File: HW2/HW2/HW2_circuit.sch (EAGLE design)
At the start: 23 parts, among them J1 PIC_ICSP_6_PIN, X1 MINI-USB_SHIELD5P2-32005-601

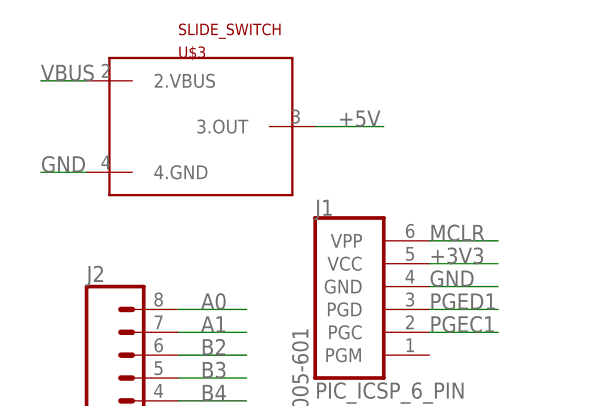
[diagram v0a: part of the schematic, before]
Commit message: Updated Library
Changed PICKIT to only have 5 through holes, modified switch connector
device to match data sheet, and changed switch and button symbols for
better illustration.
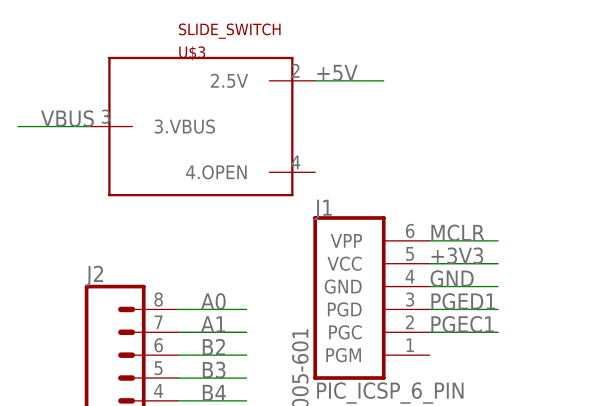
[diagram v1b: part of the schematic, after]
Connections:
- net +5V: now also U$3.2.5V; no longer U$3.3.OUT
- net GND: no longer U$3.4.GND
- net VBUS: now also U$3.3.VBUS; no longer U$3.2.VBUS
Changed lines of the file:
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@@
 </segment>
 <segment>
-<pinref part="U$3" gate="G$1" pin="3.OUT"/>
-<wire x1="-30.48" y1="60.96" x2="-22.86" y2="60.96" width="0.1524" layer="91"/>
-<label x="-27.94" y="60.96" size="1.778" layer="95"/>
+<pinref part="U$3" gate="G$1" pin="2.5V"/>
+<wire x1="-30.48" y1="66.04" x2="-22.86" y2="66.04" width="0.1524" layer="91"/>
+<label x="-30.48" y="66.04" size="1.778" layer="95"/>
 </segment>
 </net>
@@
 <label x="-15.24" y="5.08" size="1.778" layer="95"/>
 </segment>
-<segment>
-<pinref part="U$3" gate="G$1" pin="4.GND"/>
-<wire x1="-55.88" y1="55.88" x2="-60.96" y2="55.88" width="0.1524" layer="91"/>
-<label x="-60.96" y="55.88" size="1.778" layer="95"/>
-</segment>
 </net>
 <net name="OSC2" class="0">
@@
 </segment>
 <segment>
-<pinref part="U$3" gate="G$1" pin="2.VBUS"/>
-<wire x1="-55.88" y1="66.04" x2="-60.96" y2="66.04" width="0.1524" layer="91"/>
-<label x="-60.96" y="66.04" size="1.778" layer="95"/>
-</segment>
-</net>
+<pinref part="U$3" gate="G$1" pin="3.VBUS"/>
+<wire x1="-55.88" y1="60.96" x2="-63.5" y2="60.96" width="0.1524" layer="91"/>
+<label x="-60.96" y="60.96" size="1.778" layer="95"/>
+</segment>
+</net>

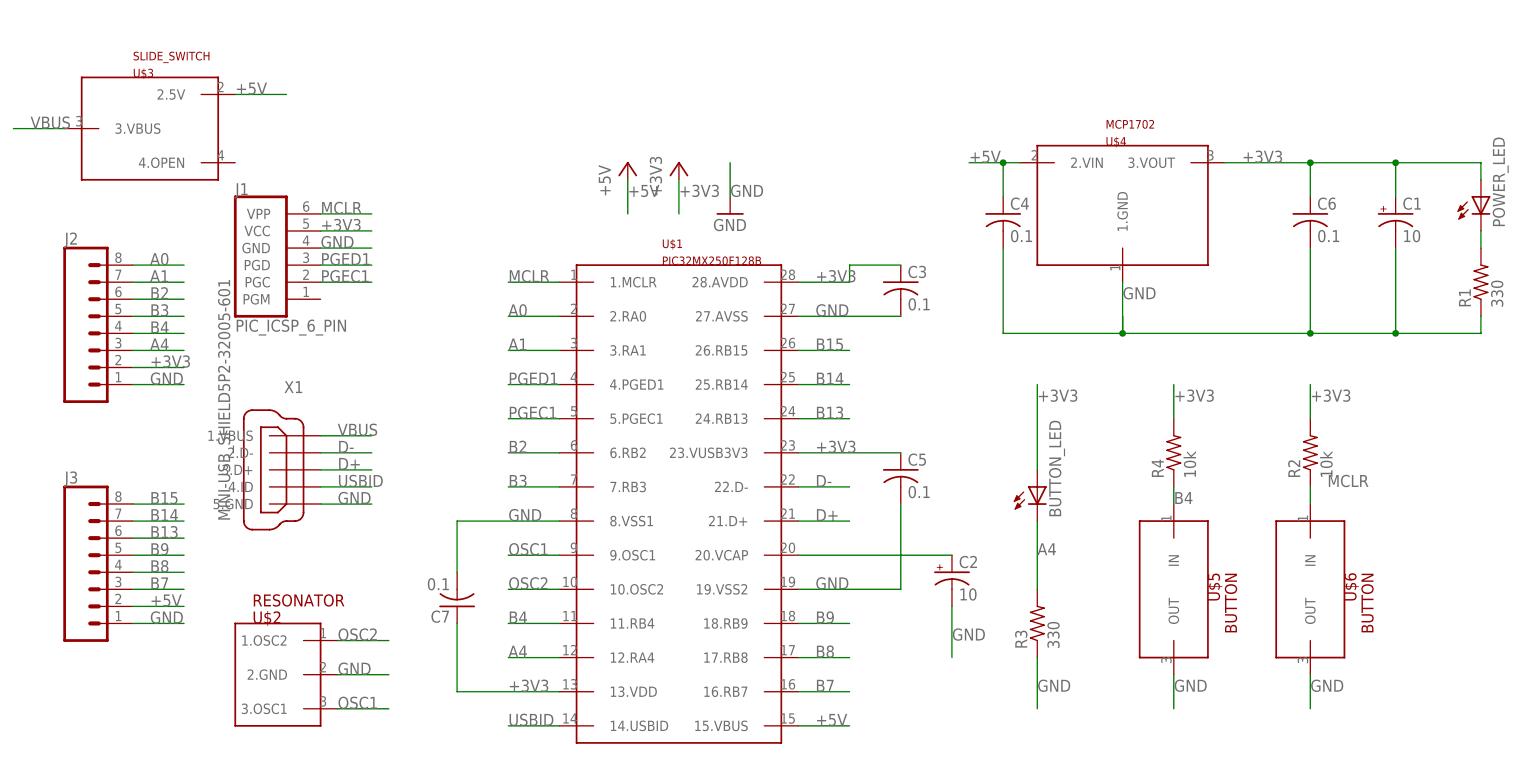
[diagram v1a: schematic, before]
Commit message: Updated Schematic Symbols
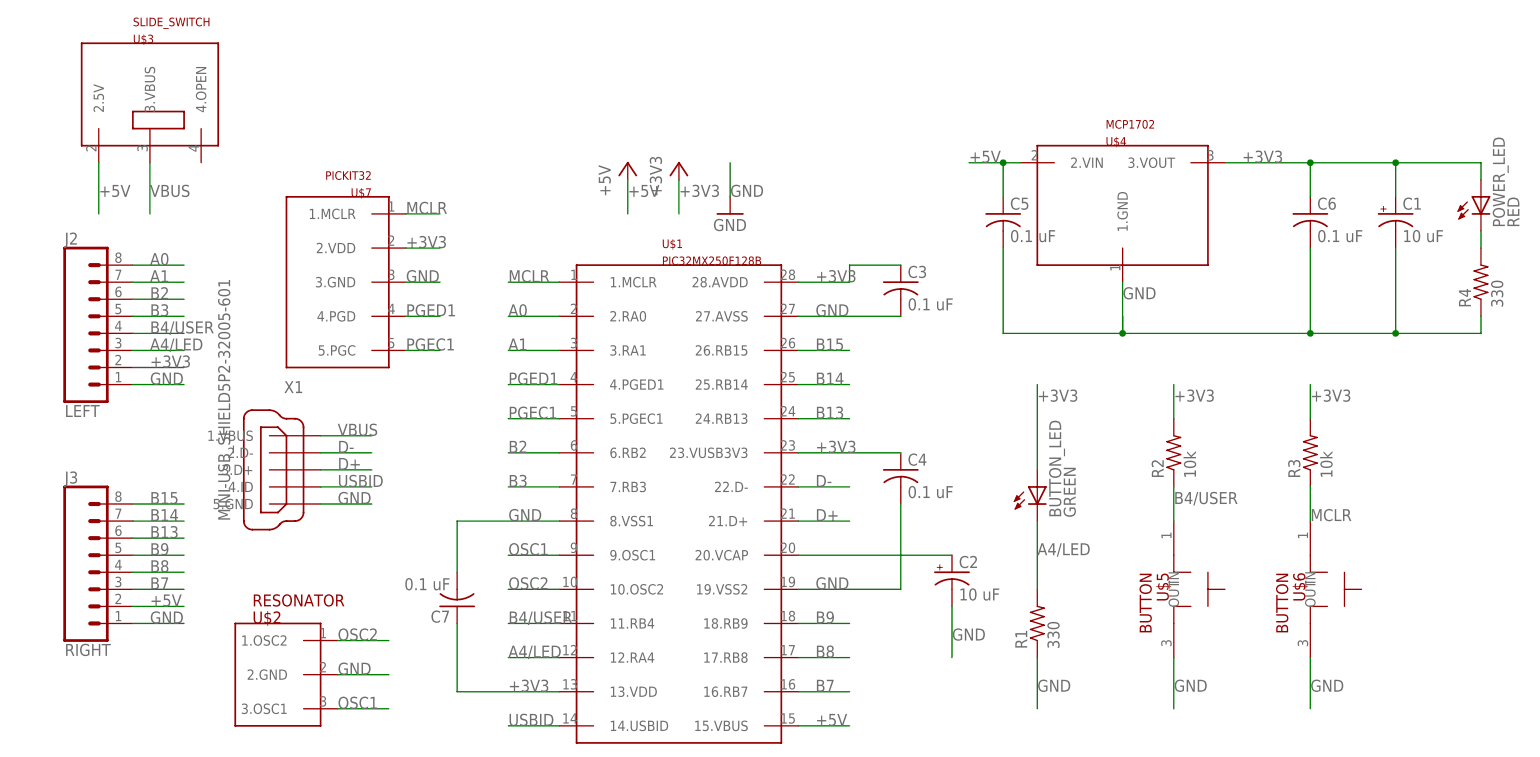
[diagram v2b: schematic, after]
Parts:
- removed J1: PIC_ICSP_6_PIN, ME433:PIC_ICSP_6_PIN
- added U$7: PICKIT32, ME433:PICKIT32
- BUTTON_LED: value (none) -> GREEN
- C1, C2: value 10 -> 10 uF
- C3, C4, C5, C6, C7: value 0.1 -> 0.1 uF; device ME433:C-US025-024X044 -> ME433:C-US025-025X050
- J2: value (none) -> LEFT
- J3: value (none) -> RIGHT
- POWER_LED: value (none) -> RED
- R1, R2: device ME433:R-US_0309/12 -> ME433:R-US_0207/10
- R3: value 330 -> 10k; device ME433:R-US_0309/12 -> ME433:R-US_0207/10
- R4: value 10k -> 330; device ME433:R-US_0309/12 -> ME433:R-US_0207/10
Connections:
- removed net A4: BUTTON_LED.C, J2.3, R3.2, U$1.12.RA4
- removed net B4: J2.4, R4.1, U$1.11.RB4, U$5.IN
- new net A4/LED: BUTTON_LED.C, J2.3, R1.2, U$1.12.RA4
- new net B4/USER: J2.4, R2.1, U$1.11.RB4, U$5.IN
- net +3V3: now also C4.1, R3.2, U$7.2.VDD; no longer C5.1, J1.VCC, R4.2
- net +5V: now also C5.1; no longer C4.1
- net GND: now also R4.1, U$7.3.GND; no longer J1.GND, R3.1
- net MCLR: now also R3.1, U$7.1.MCLR; no longer J1.VPP, R2.1
- net N$3: now also R4.2; no longer R1.2
- net PGEC1: now also U$7.5.PGC; no longer J1.PGC
- net PGED1: now also U$7.4.PGD; no longer J1.PGD
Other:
- moved on the sheet: C4, C5, R1, R2, R3, R4

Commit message: Started Board Layout
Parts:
- renumbered U$2 to 8MHZ
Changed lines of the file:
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@@
 <parts>
 <part name="U$1" library="ME433" deviceset="PIC32MX250F128B" device=""/>
-<part name="U$2" library="ME433" deviceset="RESONATOR" device=""/>
+<part name="8MHZ" library="ME433" deviceset="RESONATOR" device=""/>
 <part name="U$4" library="ME433" deviceset="MCP1702" device=""/>
 <part name="+3V1" library="ME433" deviceset="+3V3" device=""/>
@@
 <instances>
 <instance part="U$1" gate="G$1" x="35.56" y="5.08"/>
-<instance part="U$2" gate="G$1" x="-25.4" y="-20.32"/>
+<instance part="8MHZ" gate="G$1" x="-25.4" y="-20.32"/>
 <instance part="U$4" gate="G$1" x="101.6" y="53.34"/>
 <instance part="+3V1" gate="G$1" x="35.56" y="55.88"/>
@@
 </segment>
 <segment>
-<pinref part="U$2" gate="G$1" pin="2.GND"/>
+<pinref part="8MHZ" gate="G$1" pin="2.GND"/>
 <wire x1="-15.24" y1="-20.32" x2="-7.62" y2="-20.32" width="0.1524" layer="91"/>
 <label x="-15.24" y="-20.32" size="1.778" layer="95"/>
@@
 <net name="OSC2" class="0">
 <segment>
-<pinref part="U$2" gate="G$1" pin="1.OSC2"/>
+<pinref part="8MHZ" gate="G$1" pin="1.OSC2"/>
 <wire x1="-15.24" y1="-15.24" x2="-7.62" y2="-15.24" width="0.1524" layer="91"/>
 <label x="-15.24" y="-15.24" size="1.778" layer="95"/>
@@
 <net name="OSC1" class="0">
 <segment>
-<pinref part="U$2" gate="G$1" pin="3.OSC1"/>
+<pinref part="8MHZ" gate="G$1" pin="3.OSC1"/>
 <wire x1="-15.24" y1="-25.4" x2="-7.62" y2="-25.4" width="0.1524" layer="91"/>
 <label x="-15.24" y="-25.4" size="1.778" layer="95"/>

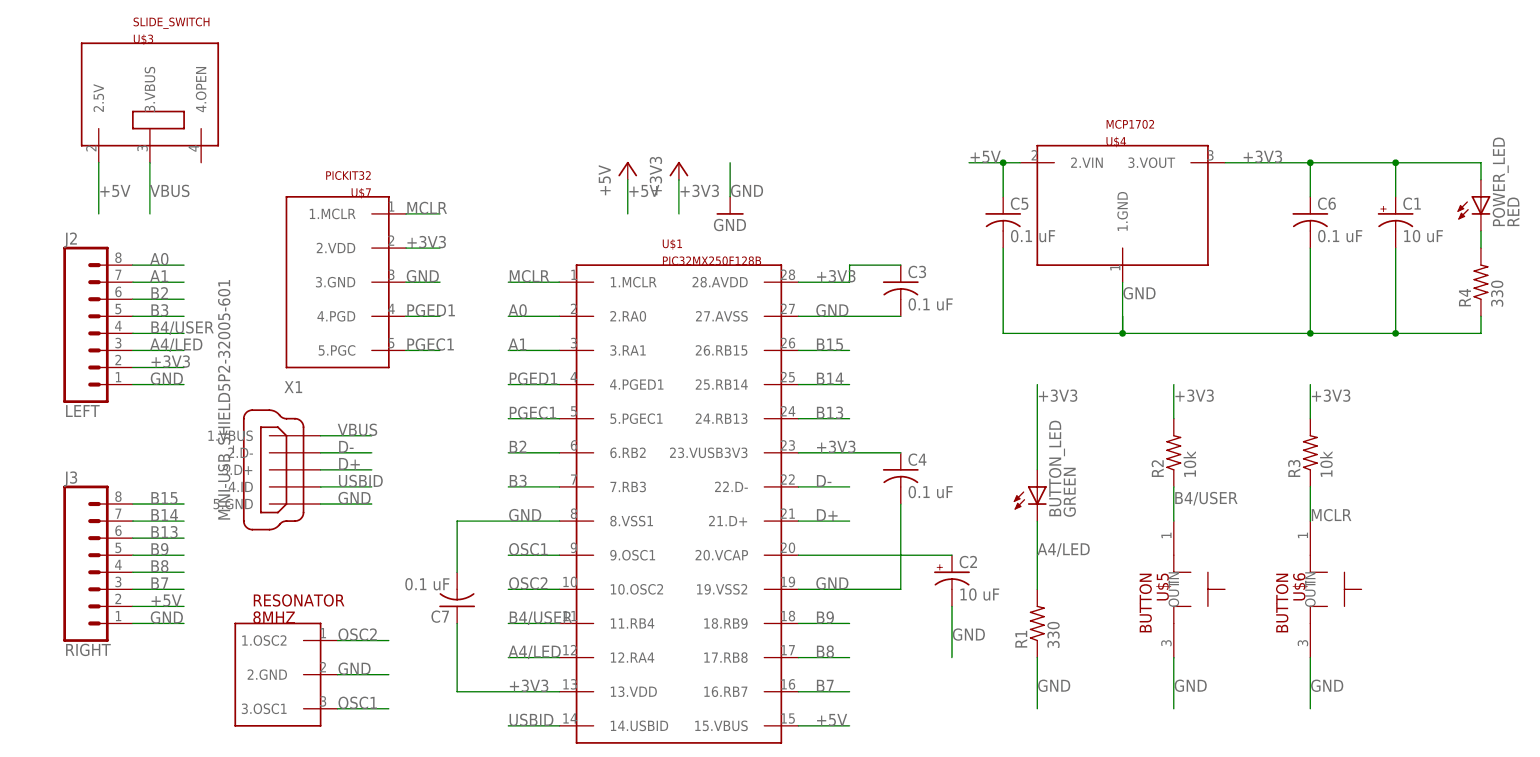
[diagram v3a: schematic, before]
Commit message: Board Layout Complete
Board layout is finished, passes DRC.  Labels have been added.
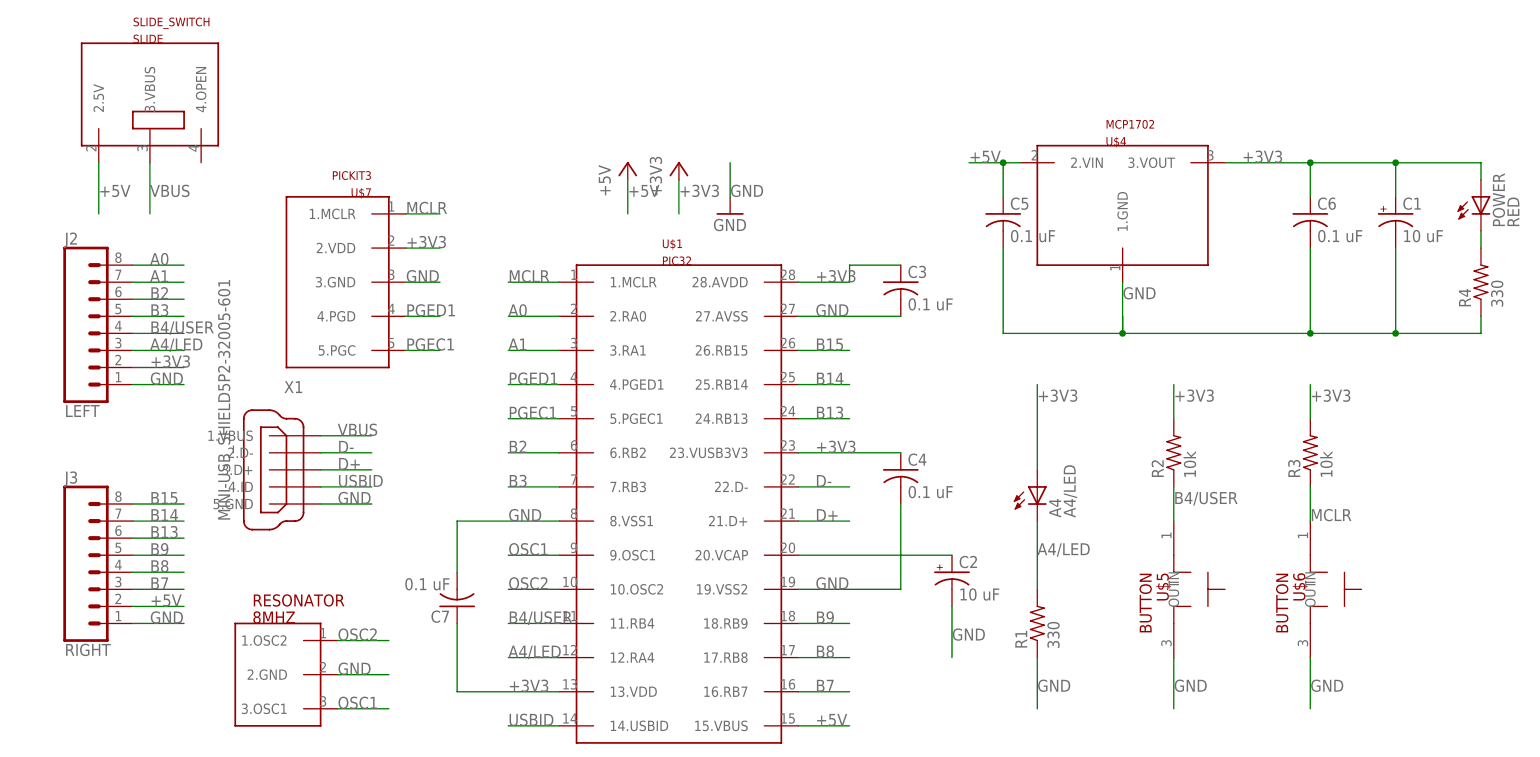
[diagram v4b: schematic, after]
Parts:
- A4: value GREEN -> A4/LED
- U$1: value PIC32MX250F128B -> PIC32
- U$7: value PICKIT32 -> PICKIT3
- renumbered BUTTON_LED to A4, POWER_LED to POWER, U$3 to SLIDE
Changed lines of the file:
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@@
 </classes>
 <parts>
-<part name="U$1" library="ME433" deviceset="PIC32MX250F128B" device=""/>
+<part name="U$1" library="ME433" deviceset="PIC32MX250F128B" device="" value="PIC32"/>
 <part name="8MHZ" library="ME433" deviceset="RESONATOR" device=""/>
 <part name="U$4" library="ME433" deviceset="MCP1702" device=""/>
@@
 <part name="U$5" library="ME433" deviceset="BUTTON" device=""/>
 <part name="GND1" library="ME433" deviceset="GND" device=""/>
-<part name="POWER_LED" library="ME433" deviceset="LED" device="3MM" value="RED"/>
-<part name="BUTTON_LED" library="ME433" deviceset="LED" device="3MM" value="GREEN"/>
+<part name="POWER" library="ME433" deviceset="LED" device="3MM" value="RED"/>
+<part name="A4" library="ME433" deviceset="LED" device="3MM" value="A4/LED"/>
 <part name="C1" library="ME433" deviceset="CPOL-US" device="B45181B" value="10 uF"/>
 <part name="C2" library="ME433" deviceset="CPOL-US" device="B45181B" value="10 uF"/>
@@
 <part name="J3" library="ME433" deviceset="CONN_08" device="&quot;" value="RIGHT"/>
 <part name="X1" library="ME433" deviceset="MINI-USB_SHIELD5P2-" device="32005-601"/>
-<part name="U$3" library="ME433" deviceset="SLIDE_SWITCH" device=""/>
-<part name="U$7" library="ME433" deviceset="PICKIT32" device=""/>
+<part name="SLIDE" library="ME433" deviceset="SLIDE_SWITCH" device=""/>
+<part name="U$7" library="ME433" deviceset="PICKIT32" device="" value="PICKIT3"/>
 <part name="R1" library="ME433" deviceset="R-US_" device="0207/10" value="330"/>
 <part name="R2" library="ME433" deviceset="R-US_" device="0207/10" value="10k"/>
@@
 <instance part="U$5" gate="G$1" x="109.22" y="-7.62" rot="R270"/>
 <instance part="GND1" gate="1" x="43.18" y="48.26"/>
-<instance part="POWER_LED" gate="G$1" x="154.94" y="50.8"/>
-<instance part="BUTTON_LED" gate="G$1" x="88.9" y="7.62"/>
+<instance part="POWER" gate="G$1" x="154.94" y="50.8"/>
+<instance part="A4" gate="G$1" x="88.9" y="7.62"/>
 <instance part="C1" gate="G$1" x="142.24" y="48.26"/>
 <instance part="C2" gate="G$1" x="76.2" y="-5.08"/>
@@
 <instance part="J3" gate="G$1" x="-50.8" y="-5.08"/>
 <instance part="X1" gate="G41" x="-22.86" y="10.16" rot="MR0"/>
-<instance part="U$3" gate="G$1" x="-43.18" y="60.96"/>
+<instance part="SLIDE" gate="G$1" x="-43.18" y="60.96"/>
 <instance part="U$7" gate="G$1" x="-15.24" y="40.64" rot="MR0"/>
 <instance part="R1" gate="G$1" x="88.9" y="-12.7" rot="R90"/>
@@
 </segment>
 <segment>
-<pinref part="U$3" gate="G$1" pin="2.5V"/>
+<pinref part="SLIDE" gate="G$1" pin="2.5V"/>
 <wire x1="-50.8" y1="55.88" x2="-50.8" y2="48.26" width="0.1524" layer="91"/>
 <label x="-50.8" y="50.8" size="1.778" layer="95"/>
@@
 <net name="N$3" class="0">
 <segment>
-<pinref part="POWER_LED" gate="G$1" pin="C"/>
+<pinref part="POWER" gate="G$1" pin="C"/>
 <wire x1="154.94" y1="45.72" x2="154.94" y2="43.18" width="0.1524" layer="91"/>
 <pinref part="R4" gate="G$1" pin="2"/>
@@
 </segment>
 <segment>
-<pinref part="BUTTON_LED" gate="G$1" pin="C"/>
+<pinref part="A4" gate="G$1" pin="C"/>
 <wire x1="88.9" y1="2.54" x2="88.9" y2="-7.62" width="0.1524" layer="91"/>
 <label x="88.9" y="-2.54" size="1.778" layer="95"/>
@@
 <wire x1="142.24" y1="55.88" x2="154.94" y2="55.88" width="0.1524" layer="91"/>
 <junction x="142.24" y="55.88"/>
-<pinref part="POWER_LED" gate="G$1" pin="A"/>
+<pinref part="POWER" gate="G$1" pin="A"/>
 <wire x1="154.94" y1="55.88" x2="154.94" y2="53.34" width="0.1524" layer="91"/>
 <pinref part="C6" gate="G$1" pin="1"/>
@@
 </segment>
 <segment>
-<pinref part="BUTTON_LED" gate="G$1" pin="A"/>
+<pinref part="A4" gate="G$1" pin="A"/>
 <wire x1="88.9" y1="10.16" x2="88.9" y2="22.86" width="0.1524" layer="91"/>
 <label x="88.9" y="20.32" size="1.778" layer="95"/>
@@
 </segment>
 <segment>
-<pinref part="U$3" gate="G$1" pin="3.VBUS"/>
+<pinref part="SLIDE" gate="G$1" pin="3.VBUS"/>
 <wire x1="-43.18" y1="55.88" x2="-43.18" y2="48.26" width="0.1524" layer="91"/>
 <label x="-43.18" y="50.8" size="1.778" layer="95"/>

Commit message: Gerber Files and Board
Board silkscreen adjusted and bmp added.  Gerber finals generated.
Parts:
- U$5: value BUTTON -> USER
- U$6: value BUTTON -> RESET
- renumbered SLIDE to ON
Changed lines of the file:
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@@
 <part name="+3V1" library="ME433" deviceset="+3V3" device=""/>
 <part name="P+1" library="ME433" deviceset="+5V" device=""/>
-<part name="U$5" library="ME433" deviceset="BUTTON" device=""/>
+<part name="U$5" library="ME433" deviceset="BUTTON" device="" value="USER"/>
 <part name="GND1" library="ME433" deviceset="GND" device=""/>
 <part name="POWER" library="ME433" deviceset="LED" device="3MM" value="RED"/>
@@
 <part name="C1" library="ME433" deviceset="CPOL-US" device="B45181B" value="10 uF"/>
 <part name="C2" library="ME433" deviceset="CPOL-US" device="B45181B" value="10 uF"/>
-<part name="U$6" library="ME433" deviceset="BUTTON" device=""/>
+<part name="U$6" library="ME433" deviceset="BUTTON" device="" value="RESET"/>
 <part name="J2" library="ME433" deviceset="CONN_08" device="&quot;" value="LEFT"/>
 <part name="J3" library="ME433" deviceset="CONN_08" device="&quot;" value="RIGHT"/>
 <part name="X1" library="ME433" deviceset="MINI-USB_SHIELD5P2-" device="32005-601"/>
-<part name="SLIDE" library="ME433" deviceset="SLIDE_SWITCH" device=""/>
+<part name="ON" library="ME433" deviceset="SLIDE_SWITCH" device=""/>
 <part name="U$7" library="ME433" deviceset="PICKIT32" device="" value="PICKIT3"/>
 <part name="R1" library="ME433" deviceset="R-US_" device="0207/10" value="330"/>
@@
 <instance part="J3" gate="G$1" x="-50.8" y="-5.08"/>
 <instance part="X1" gate="G41" x="-22.86" y="10.16" rot="MR0"/>
-<instance part="SLIDE" gate="G$1" x="-43.18" y="60.96"/>
+<instance part="ON" gate="G$1" x="-43.18" y="60.96"/>
 <instance part="U$7" gate="G$1" x="-15.24" y="40.64" rot="MR0"/>
 <instance part="R1" gate="G$1" x="88.9" y="-12.7" rot="R90"/>
@@
 </segment>
 <segment>
-<pinref part="SLIDE" gate="G$1" pin="2.5V"/>
+<pinref part="ON" gate="G$1" pin="2.5V"/>
 <wire x1="-50.8" y1="55.88" x2="-50.8" y2="48.26" width="0.1524" layer="91"/>
 <label x="-50.8" y="50.8" size="1.778" layer="95"/>
@@
 </segment>
 <segment>
-<pinref part="SLIDE" gate="G$1" pin="3.VBUS"/>
+<pinref part="ON" gate="G$1" pin="3.VBUS"/>
 <wire x1="-43.18" y1="55.88" x2="-43.18" y2="48.26" width="0.1524" layer="91"/>
 <label x="-43.18" y="50.8" size="1.778" layer="95"/>
